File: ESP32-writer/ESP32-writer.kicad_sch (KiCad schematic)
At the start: 12 parts, among them J1 USB2.0_C, J2 UART-OUTPUT, Q1 2N7000, Q2 2N7000, U1 CH340C

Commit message: esp32-writer
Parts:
- added C4: 10u, $74th:Capacitor_0805_2012, symbol Device:C
- added D2: D_Schottky, $74th:D_SMA, symbol Device:D_Schottky
- added J3: USB2.0_C, $74th:USB-C-12-Pin-MidMount-ali-v4, symbol esp32-dev-board:USB2.0_C
- added R4, R5: 5.1k, $74th:Register_0805_2012, symbol Device:R
- C1, C2, C3: footprint (none) -> $74th:Capacitor_0805_2012
- D1: footprint (none) -> $74th:LED_0805_2012Metric_Pad1.15x1.40mm_HandSolder
- J1: footprint (none) -> $74th:USB-C-12-Pin-MidMount-ali-v4
- J2: footprint (none) -> esp32-dev-board:UART
- Q1, Q2: value 2N7000 -> 2N7002; footprint Package_TO_SOT_THT:TO-92_Inline -> Package_TO_SOT_SMD:SOT-23
- R1, R2, R3: footprint (none) -> $74th:Register_0805_2012
- U1: footprint (none) -> Package_SO:SOP-16_3.9x9.9mm_P1.27mm
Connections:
- net +5V: now also C4.1, D2.1 (K)
- net DM: now also J3.2 (D-); no longer J1.2 (D-)
- net DP: now also J3.3 (D+); no longer J1.3 (D+)
- net GND: now also C4.2, J3.4 (GND), R4.2, R5.2
- net +3V3: now reaches C2.1, U1.4 (V3)
- new net: D2.2 (A), J3.1 (VBUS)
- new net: J3.5 (CC1), R4.1
- new net: J3.6 (CC2), R5.1
- no-connect marks 6 -> 8
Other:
- moved on the sheet: C1, J1, R1, R2

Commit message: up
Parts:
- removed Q1, Q2: 2N7002, Package_TO_SOT_SMD:SOT-23, symbol Transistor_FET:2N7000
- added Q1, Q2: 2N7002, Package_TO_SOT_SMD:SOT-23, symbol Transistor_FET:2N7002
- added U2: ESP-Prog-ProgramCOM-SEND, $74th:BoxPinHeader_2x03_P1.27mm_Vertical, symbol $74th:ESP-Prog-ProgramCOM-SEND
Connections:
- net +5V: now also U2.2 (VCC)
- net BOOT: now also Q2.3 (D), U2.6 (IO0)
- net GND: now also U2.4 (GND)
- net RESET: now also Q1.3 (D), U2.1 (EN)
- net RTS: now also Q1.2 (S), Q2.1 (G)
- net RXD: now also U2.5 (RXD0)
- net TXD: now also U2.3 (TXD0)
- net DTS renamed DTR
- net DTR: now also Q1.1 (G), Q2.2 (S)

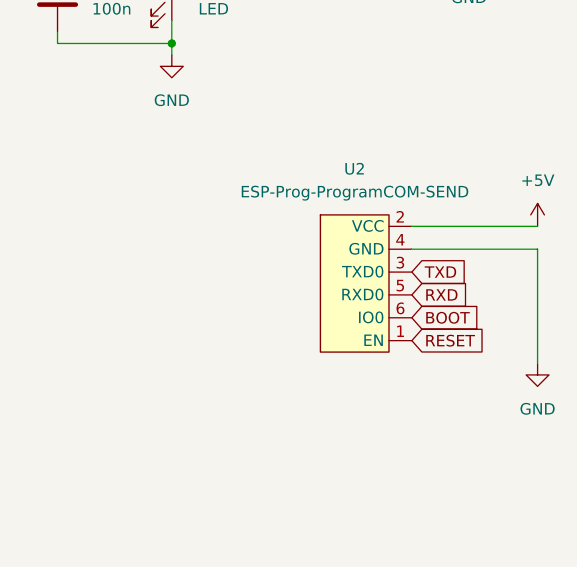
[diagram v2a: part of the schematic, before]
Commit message: ESP32-C3-WROOM-02
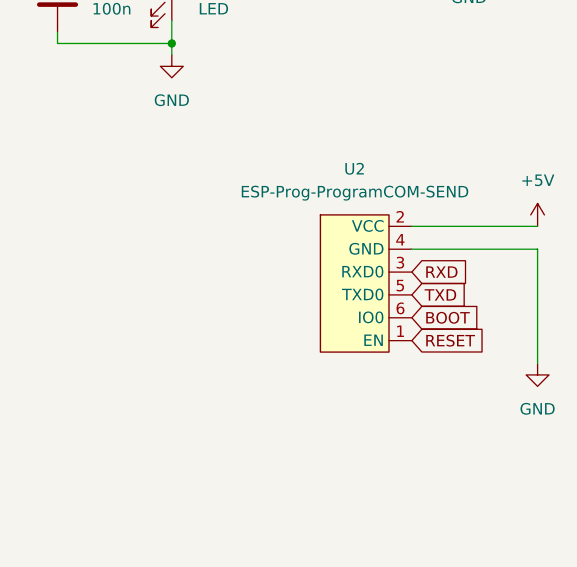
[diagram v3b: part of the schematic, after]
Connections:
- net RXD: now also U2.3 (RXD0); no longer U2.5 (RXD0)
- net TXD: now also U2.5 (TXD0); no longer U2.3 (TXD0)
- net +3V3 renamed +3.3V
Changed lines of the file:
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@@
     )
   )
-  (global_label "TXD" (shape input) (at 217.17 107.95 0) (fields_autoplaced)
+  (global_label "TXD" (shape input) (at 217.17 110.49 0) (fields_autoplaced)
     (effects (font (size 1.27 1.27)) (justify left))
-    (property "シート間のリファレンス" "${INTERSHEET_REFS}" (id 0) (at 223.0302 107.8706 0)
+    (property "シート間のリファレンス" "${INTERSHEET_REFS}" (id 0) (at 223.0302 110.4106 0)
       (effects (font (size 1.27 1.27)) (justify left) hide)
     )
@@
     )
   )
-  (global_label "RXD" (shape input) (at 217.17 110.49 0) (fields_autoplaced)
+  (global_label "RXD" (shape input) (at 217.17 107.95 0) (fields_autoplaced)
     (effects (font (size 1.27 1.27)) (justify left))
-    (property "シート間のリファレンス" "${INTERSHEET_REFS}" (id 0) (at 223.3326 110.4106 0)
+    (property "シート間のリファレンス" "${INTERSHEET_REFS}" (id 0) (at 223.3326 107.8706 0)
       (effects (font (size 1.27 1.27)) (justify left) hide)
     )

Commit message: update ESP32-Writer
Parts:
- added C5: 10u, $74th:Capacitor_0805_2012, symbol Device:C
- added C6, C7: 22p, $74th:Capacitor_0805_2012, symbol Device:C
- added F1, F2: Polyfuse, symbol Device:Polyfuse
- added SW1: SW_DPDT_x2, symbol Switch:SW_DPDT_x2
- added U3: Regulator_PQ033EZ1HZ, symbol esp32-dev-board:Regulator_PQ033EZ1HZ
- added Y1: Crystal_GND24, symbol Device:Crystal_GND24
- U1: symbol esp32-dev-board:CH340C -> esp32-dev-board:CH340G
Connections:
- net +5V: now also F2.2, U3.1 (VIN); no longer J1.1 (VBUS)
- net GND: now also C5.2, C6.1, C7.1, U3.5 (GND)
- net at D2.2 (A): now also F1.2; no longer J3.1 (VBUS)
- net at U1.7 (XI): now also Y1.3
- net at U1.8 (XO): now also Y1.1
- net +3.3V: no longer names the net of C2.1
- net +3.3V: now also SW1.1 (A); no longer U1.4 (V3)
- new net: C6.2, Y1.2
- new net: C7.2, Y1.4
- new net: F1.1, J3.1 (VBUS)
- new net: SW1.2 (B), U1.4 (V3)
- new net: F2.1, J1.1 (VBUS)
- new net +3V3: C5.1, SW1.3 (C), U3.3 (VOUT)
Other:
- moved on the sheet: C1, C2, C3, C4, D1, D2, J1, J2, J3, R1, R2, R3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

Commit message: up
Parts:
- removed U3: Regulator_PQ033EZ1HZ, symbol esp32-dev-board:Regulator_PQ033EZ1HZ
- added U4: AMS1117-3.3, Package_TO_SOT_SMD:SOT-223-3_TabPin2, symbol Regulator_Linear:AMS1117-3.3
- F1, F2: footprint (none) -> $74th:ResettableFuse_KT6-1100SMDI
- U1: value CH340C -> CH340G
- Y1: footprint (none) -> $74th:Crystal_SMD_3215-2Pin_3.2x1.5mm
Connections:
- net +3V3: now also U4.2 (VO)
- net +5V: now also U4.3 (VI)
- net GND: now also U4.1 (GND)
- no-connect marks 8 -> 7
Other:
- moved on the sheet: J2, Q1, Q2, U2

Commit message: up
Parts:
- removed SW1: SW_DPDT_x2, symbol Switch:SW_DPDT_x2
- added C4: C, $74th:Capacitor_0805_2012, symbol Device:C
- added JP1: Jumper_3_Open, symbol Jumper:Jumper_3_Open
- C1: value 10u -> C
- C2: renamed from C4; value 10u -> C
- C3: renamed from C5; value 10u -> C
- C5: renamed from C2; value 100n -> C
- C6, C7: value 22p -> C
- C8: renamed from C3; value 100n -> C
- R1: value 5.1k -> R
- R2: renamed from R4; value 5.1k -> R
- R3: renamed from R2; value 5.1k -> R
- R4: renamed from R5; value 5.1k -> R
- R5: renamed from R3; value 1k -> R
- renumbered D2 to D1, D1 to D2, J3 to J2, J2 to J3, U2 to J4, U4 to U1, U1 to U2
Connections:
- net +3V3: now also JP1.3 (B)
- net GND: now also C4.2
- net RESET: now also C4.1
- net at C5.1: now also JP1.1 (A)
- net at U2.4 (V3): now also JP1.2 (C)
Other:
- moved on the sheet: C5

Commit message: update esp32-writer
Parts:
- removed C2: C, $74th:Capacitor_0805_2012, symbol Device:C
- added JP3: Jumper_2_Open, Jumper:SolderJumper-2_P1.3mm_Open_RoundedPad1.0x1.5mm, symbol Jumper:Jumper_2_Open
- C1, C3, C8: value C -> 1u
- C4, C5: value C -> 100n
- C6, C7: value C -> 22p
- J1, J2: footprint $74th:USB-C-12-Pin-MidMount-ali-v4 -> $74th:USB-C-12-Pin-MidMount-ali-v5
- J3: symbol esp32-dev-board:UART-OUTPUT -> esp32-dev-board:UART-OUTPUT-v2
- JP1: footprint (none) -> Jumper:SolderJumper-3_P1.3mm_Open_RoundedPad1.0x1.5mm_NumberLabels
- R1, R2, R3, R4: value R -> 5.1k
- R5: value R -> 200
- U2: symbol esp32-dev-board:CH340G -> $74th:CH340G
- Y1: value Crystal_GND24 -> 12M; footprint $74th:Crystal_SMD_3215-2Pin_3.2x1.5mm -> $74th:Crystal_SMD_3225-4Pin_3.2x2.5mm_HandSoldering
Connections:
- net +3V3: now also J3.4 (3V3), JP1.1 (A), JP3.1 (A); no longer JP1.3 (B)
- net BOOT: now also J3.7 (BOOT); no longer J3.6 (BOOT)
- net GND: now also J3.5 (GND); no longer J3.4 (GND)
- net RESET: now also J3.6 (EN); no longer J3.5 (EN)
- net at C5.1: now also JP1.3 (B); no longer JP1.1 (A)
- net at U2.15 (R232): now also JP3.2 (B)
- no-connect marks 7 -> 6
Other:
- moved on the sheet: C5, C6, C7, C8, D2, JP1, R5, Y1

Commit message: type-b
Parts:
- renumbered C5 to C2, C7 to C3, C8 to C4, C6 to C5, C3 to C6, C4 to C7, F2 to F1, F1 to F2, J4 to J3, J3 to J4, JP3 to JP2, Q2 to Q1, Q1 to Q2, R5 to R1, R4 to R3, R1 to R4, R3 to R5
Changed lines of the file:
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@@
   (symbol (lib_id "Device:R") (at 234.95 72.39 0) (unit 1)
     (in_bom yes) (on_board yes) (dnp no)
-    (property "Reference" "R5" (at 237.49 71.1199 0)
+    (property "Reference" "R1" (at 237.49 71.1199 0)
       (effects (font (size 1.27 1.27)) (justify left))
     )
@@
       (project "ESP32-writer"
         (path "/7a6a2881-36a3-49f9-9509-bb2f48ffa349"
-          (reference "R5") (unit 1)
+          (reference "R1") (unit 1)
         )
       )
@@
   (symbol (lib_id "Device:C") (at 114.3 134.62 0) (unit 1)
     (in_bom yes) (on_board yes) (dnp no) (fields_autoplaced)
-    (property "Reference" "C4" (at 118.11 133.3499 0)
+    (property "Reference" "C7" (at 118.11 133.3499 0)
       (effects (font (size 1.27 1.27)) (justify left))
     )
@@
       (project "ESP32-writer"
         (path "/7a6a2881-36a3-49f9-9509-bb2f48ffa349"
-          (reference "C4") (unit 1)
+          (reference "C7") (unit 1)
         )
       )
@@
   (symbol (lib_id "Device:C") (at 113.03 60.96 0) (unit 1)
     (in_bom yes) (on_board yes) (dnp no)
-    (property "Reference" "C3" (at 116.84 59.6899 0)
+    (property "Reference" "C6" (at 116.84 59.6899 0)
       (effects (font (size 1.27 1.27)) (justify left))
     )
@@
       (project "ESP32-writer"
         (path "/7a6a2881-36a3-49f9-9509-bb2f48ffa349"
-          (reference "C3") (unit 1)
+          (reference "C6") (unit 1)
         )
       )
@@
   (symbol (lib_id "$74th:ESP-Prog-ProgramCOM-SEND") (at 194.31 135.89 0) (unit 1)
     (in_bom yes) (on_board yes) (dnp no) (fields_autoplaced)
-    (property "Reference" "J4" (at 194.31 127 0)
+    (property "Reference" "J3" (at 194.31 127 0)
       (effects (font (size 1.27 1.27)))
     )
@@
       (project "ESP32-writer"
         (path "/7a6a2881-36a3-49f9-9509-bb2f48ffa349"
-          (reference "J4") (unit 1)
+          (reference "J3") (unit 1)
         )
       )
@@
   (symbol (lib_id "Device:R") (at 52.07 81.28 0) (unit 1)
     (in_bom yes) (on_board yes) (dnp no) (fields_autoplaced)
-    (property "Reference" "R1" (at 54.61 80.0099 0)
+    (property "Reference" "R4" (at 54.61 80.0099 0)
       (effects (font (size 1.27 1.27)) (justify left))
     )
@@
       (project "ESP32-writer"
         (path "/7a6a2881-36a3-49f9-9509-bb2f48ffa349"
-          (reference "R1") (unit 1)
+          (reference "R4") (unit 1)
         )
       )
@@
   (symbol (lib_id "esp32-dev-board:UART-OUTPUT-v2") (at 194.31 99.06 0) (unit 1)
     (in_bom yes) (on_board yes) (dnp no) (fields_autoplaced)
-    (property "Reference" "J3" (at 196.215 95.25 0)
+    (property "Reference" "J4" (at 196.215 95.25 0)
       (effects (font (size 1.27 1.27)))
     )
@@
       (project "ESP32-writer"
         (path "/7a6a2881-36a3-49f9-9509-bb2f48ffa349"
-          (reference "J3") (unit 1)
+          (reference "J4") (unit 1)
         )
       )
@@
   (symbol (lib_id "Device:C") (at 165.1 90.17 180) (unit 1)
     (in_bom yes) (on_board yes) (dnp no)
-    (property "Reference" "C7" (at 170.18 88.9 0)
+    (property "Reference" "C3" (at 170.18 88.9 0)
       (effects (font (size 1.27 1.27)) (justify right))
     )
@@
       (project "ESP32-writer"
         (path "/7a6a2881-36a3-49f9-9509-bb2f48ffa349"
-          (reference "C7") (unit 1)
+          (reference "C3") (unit 1)
         )
       )
@@
   (symbol (lib_id "Device:C") (at 190.5 45.72 0) (unit 1)
     (in_bom yes) (on_board yes) (dnp no)
-    (property "Reference" "C8" (at 194.31 44.45 0)
+    (property "Reference" "C4" (at 194.31 44.45 0)
       (effects (font (size 1.27 1.27)) (justify left))
     )
@@
       (project "ESP32-writer"
         (path "/7a6a2881-36a3-49f9-9509-bb2f48ffa349"
-          (reference "C8") (unit 1)
+          (reference "C4") (unit 1)
         )
       )
@@
   (symbol (lib_id "Device:R") (at 63.5 129.54 0) (unit 1)
     (in_bom yes) (on_board yes) (dnp no) (fields_autoplaced)
-    (property "Reference" "R4" (at 66.04 128.2699 0)
+    (property "Reference" "R3" (at 66.04 128.2699 0)
       (effects (font (size 1.27 1.27)) (justify left))
     )
@@
       (project "ESP32-writer"
         (path "/7a6a2881-36a3-49f9-9509-bb2f48ffa349"
-          (reference "R4") (unit 1)
+          (reference "R3") (unit 1)
         )
       )
@@
   (symbol (lib_id "Jumper:Jumper_2_Open") (at 165.1 60.96 270) (unit 1)
     (in_bom yes) (on_board yes) (dnp no) (fields_autoplaced)
-    (property "Reference" "JP3" (at 167.64 60.325 90)
+    (property "Reference" "JP2" (at 167.64 60.325 90)
       (effects (font (size 1.27 1.27)) (justify left))
     )
@@
       (project "ESP32-writer"
         (path "/7a6a2881-36a3-49f9-9509-bb2f48ffa349"
-          (reference "JP3") (unit 1)
+          (reference "JP2") (unit 1)
         )
       )
@@
   (symbol (lib_id "Device:C") (at 149.86 88.9 180) (unit 1)
     (in_bom yes) (on_board yes) (dnp no)
-    (property "Reference" "C6" (at 144.78 87.63 0)
+    (property "Reference" "C5" (at 144.78 87.63 0)
       (effects (font (size 1.27 1.27)))
     )
@@
       (project "ESP32-writer"
         (path "/7a6a2881-36a3-49f9-9509-bb2f48ffa349"
-          (reference "C6") (unit 1)
+          (reference "C5") (unit 1)
         )
       )
@@
   (symbol (lib_id "Transistor_FET:2N7002") (at 140.97 142.24 0) (mirror x) (unit 1)
     (in_bom yes) (on_board yes) (dnp no) (fields_autoplaced)
-    (property "Reference" "Q2" (at 147.32 140.9699 0)
+    (property "Reference" "Q1" (at 147.32 140.9699 0)
       (effects (font (size 1.27 1.27)) (justify left))
     )
@@
       (project "ESP32-writer"
         (path "/7a6a2881-36a3-49f9-9509-bb2f48ffa349"
-          (reference "Q2") (unit 1)
+          (reference "Q1") (unit 1)
         )
       )
@@
   (symbol (lib_id "Device:Polyfuse") (at 55.88 105.41 90) (unit 1)
     (in_bom yes) (on_board yes) (dnp no) (fields_autoplaced)
-    (property "Reference" "F1" (at 55.88 99.06 90)
+    (property "Reference" "F2" (at 55.88 99.06 90)
       (effects (font (size 1.27 1.27)))
     )
@@
       (project "ESP32-writer"
         (path "/7a6a2881-36a3-49f9-9509-bb2f48ffa349"
-          (reference "F1") (unit 1)
+          (reference "F2") (unit 1)
         )
       )
@@
   (symbol (lib_id "Device:Polyfuse") (at 58.42 57.15 90) (unit 1)
     (in_bom yes) (on_board yes) (dnp no) (fields_autoplaced)
-    (property "Reference" "F2" (at 58.42 50.8 90)
+    (property "Reference" "F1" (at 58.42 50.8 90)
       (effects (font (size 1.27 1.27)))
     )
@@
       (project "ESP32-writer"
         (path "/7a6a2881-36a3-49f9-9509-bb2f48ffa349"
-          (reference "F2") (unit 1)
+          (reference "F1") (unit 1)
         )
       )
@@
   (symbol (lib_id "Device:C") (at 223.52 54.61 0) (unit 1)
     (in_bom yes) (on_board yes) (dnp no) (fields_autoplaced)
-    (property "Reference" "C5" (at 227.33 53.3399 0)
+    (property "Reference" "C2" (at 227.33 53.3399 0)
       (effects (font (size 1.27 1.27)) (justify left))
     )
@@
       (project "ESP32-writer"
         (path "/7a6a2881-36a3-49f9-9509-bb2f48ffa349"
-          (reference "C5") (unit 1)
+          (reference "C2") (unit 1)
         )
       )
@@
   (symbol (lib_id "Transistor_FET:2N7002") (at 140.97 125.73 0) (mirror x) (unit 1)
     (in_bom yes) (on_board yes) (dnp no) (fields_autoplaced)
-    (property "Reference" "Q1" (at 147.32 124.4599 0)
+    (property "Reference" "Q2" (at 147.32 124.4599 0)
       (effects (font (size 1.27 1.27)) (justify left))
     )
@@
       (project "ESP32-writer"
         (path "/7a6a2881-36a3-49f9-9509-bb2f48ffa349"
-          (reference "Q1") (unit 1)
+          (reference "Q2") (unit 1)
         )
       )
@@
   (symbol (lib_id "Device:R") (at 62.23 81.28 0) (unit 1)
     (in_bom yes) (on_board yes) (dnp no) (fields_autoplaced)
-    (property "Reference" "R3" (at 64.77 80.0099 0)
+    (property "Reference" "R5" (at 64.77 80.0099 0)
       (effects (font (size 1.27 1.27)) (justify left))
     )
@@
       (project "ESP32-writer"
         (path "/7a6a2881-36a3-49f9-9509-bb2f48ffa349"
-          (reference "R3") (unit 1)
-        )
-      )
+          (reference "R5") (unit 1)
+        )
+      )
